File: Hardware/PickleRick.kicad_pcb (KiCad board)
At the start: 6 copper layers, 100 x 37 mm, 218 parts, among them IC1 MIC5060YML-TR, J1 RBUS, J10 Conn_Coaxial, J11 Conn_Coaxial, J12 Conn_01x03_Male, J13 Conn_01x03_Pin, J14 Conn_01x07_Socket, J2 Conn_01x02_Male, J3 ST1W008S4TR2000, J4 Conn_01x03_Pin, J5 USB_C_Receptacle_USB2.0, J6 Screw_Terminal_01x08, J7 Conn_01x05_Male, J8 DeployLipo, J9 UCLipo, Q1 PMV20ENR, Q10 DMP3099L, Q11 SQS141ELNW-T1_GE3, Q12 SQS141ELNW-T1_GE3, Q2 BSZ025N04LS, Q3 BSZ025N04LS, Q4 BSZ025N04LS, Q5 BSZ025N04LS, Q6 BSZ025N04LS, Q8 DMP3099L, Q9 DMP3099L, U1 ESP32-S3, U10 LTC4412xS6, U11 MP28167GQ-A-Z, U12 INA219AxDCN, U14 LTC4412xS6, U16 SC4215, U17 LTC4412xS6, U19 MAX-M10S, U2 DPS368, U20 SN65HVD230, U21 RFM95W-868S2, U22 LTC4412xS6, U3 LTV-247, U4 PCA9534RGVR, U5 PCA9685BS, U6 H3LIS331DLTR, U7 ICM-20608-G, U8 MMC5983MA, U9 LTC4412xS6, Y1 R940000171

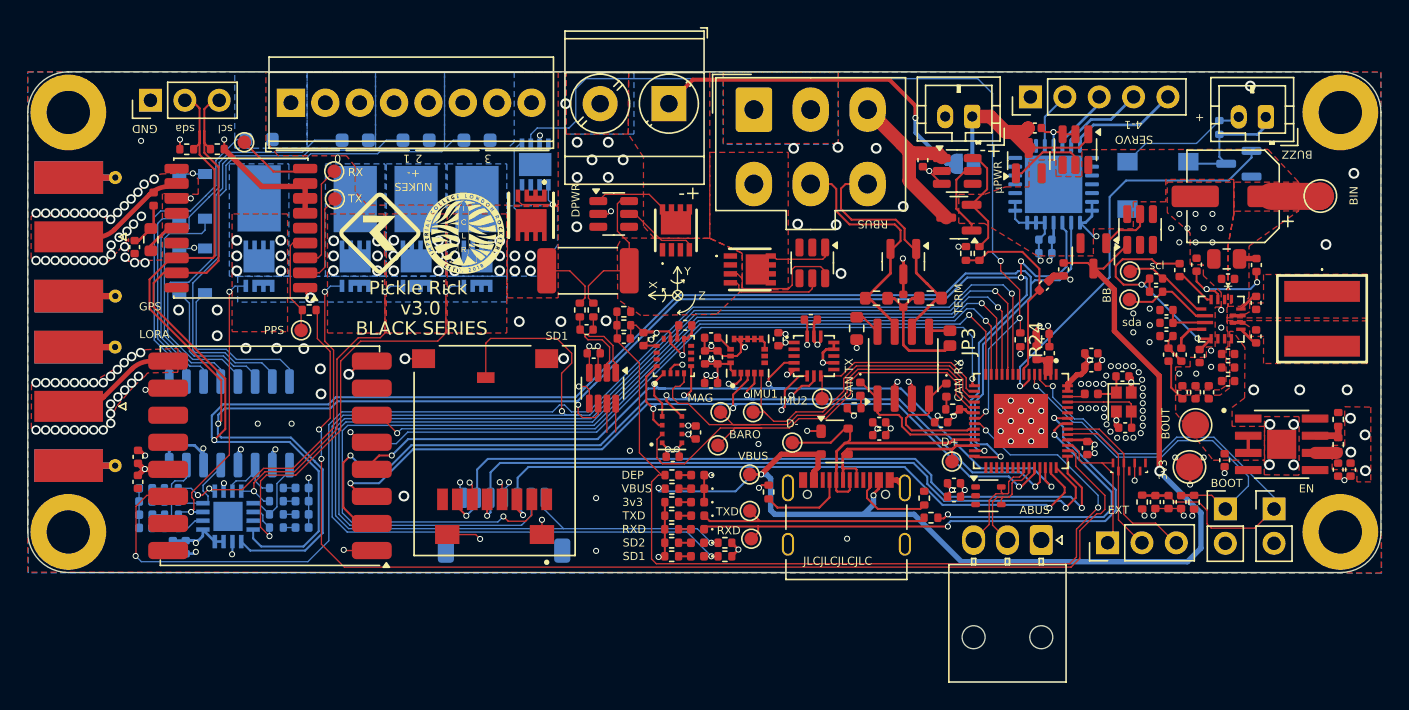
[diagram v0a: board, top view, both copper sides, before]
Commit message: updated hardware with current limitng resistors on pwm outputs
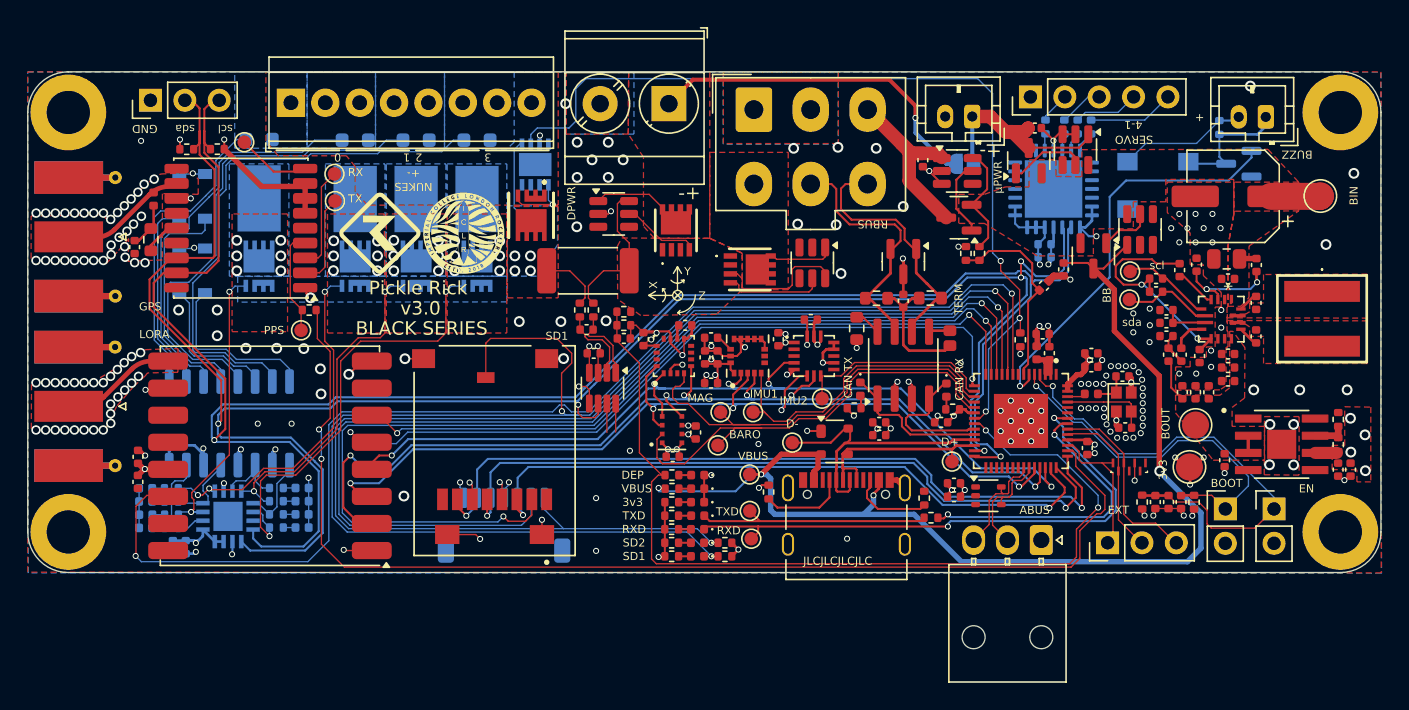
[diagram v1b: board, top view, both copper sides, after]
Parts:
- added R47: 220, Resistor_SMD:R_0402_1005Metric, B.Cu at (178.6, 64.1)
- added R52: 220, Resistor_SMD:R_0402_1005Metric, B.Cu at (177.6, 64.1)
- added R53: 220, Resistor_SMD:R_0402_1005Metric, B.Cu at (176.6, 64.1)
- added R54: 220, Resistor_SMD:R_0402_1005Metric, B.Cu at (175.2, 64.1)
- moved C19 0.34 mm to (175.1, 72.7)
- moved U5 0.34 mm to (175.8, 68.7)
- moved C20 0.30 mm to (175.1, 73.7)
- moved TP5 0.19 mm to (122.7, 67.5)
- moved TP6 0.15 mm to (122.7, 69.5)
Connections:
- J7 pad 2: /nukes/SERVO0 -> Net-(J7-Pin_2)
- J7 pad 3: /nukes/SERVO1 -> Net-(J7-Pin_3)
- J7 pad 4: /nukes/SERVO2 -> Net-(J7-Pin_4)
- J7 pad 5: /nukes/SERVO3 -> Net-(J7-Pin_5)
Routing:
- net /nukes/SERVO3: track 8.33 -> 1.58 mm
- net Net-(J7-Pin_5): track 0.00 -> 6.39 mm
- net /nukes/SERVO2: track 6.39 -> 1.44 mm
- net Net-(J7-Pin_4): track 0.00 -> 4.84 mm
- net Net-(J7-Pin_3): track 0.00 -> 3.29 mm
- net /nukes/SERVO0: track 4.24 -> 1.26 mm
- net /nukes/SERVO1: track 3.85 -> 1.29 mm
- net Net-(J7-Pin_2): track 0.00 -> 2.30 mm

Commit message: update
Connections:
- U12 pad 7: GND -> +3V3
- U12 pad 8: GND -> +3V3
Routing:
- net +3V3: track 82.5 -> 93.3 mm
- net GND: track 112.4 -> 108.1 mm

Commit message: Ordering v3
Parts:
- added E1: SparkGap, iclr:Spark_Gap, F.Cu at (107.3, 71.8)
- IC1: footprint iclr-hw:SON65P300X300X100-9N-D -> iclr:SON65P300X300X100-9N-D
- J5: footprint Connector_USB:USB_C_Receptacle_Palconn_UTC16-G -> iclr:USB_C_Receptacle_Palconn_UTC16-G
- Y1: footprint Crystal:Crystal_SMD_2016-4Pin_2.0x1.6mm -> iclr:Crystal_SMD_2016-4Pin_2.0x1.6mm
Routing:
- net /power/UC_Lipo+: track 15.0 -> 12.6 mm
- net /power/RBUS_3.3V_IN: track 14.7 -> 13.5 mm
- net GND: vias 224 -> 223
- added copper zone on F.Cu, net /power/RBUS_3.3V_IN
- added copper zone on F.Cu, net /power/UC_Lipo+
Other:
- board text removed: "JLCJLCJLCJLC"
